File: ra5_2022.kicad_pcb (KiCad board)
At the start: 2 copper layers, 178 parts, among them CN1 KF250-3.5-2P-2, CN2 MX15EDGRHC-3.5-2*02P-BK01-CU-A, CN3 KF250-3.5-2P-2, CN4 KF250-3.5-2P-2, J2 MX15EDGRHC-3.5-2x03P, Q2 BC817, Q3 BC817, Q4 BC817, Q5 BC817, Q6 BC817, U1 TPS54202DDC, U10 DB126V-5.0-2P-BK-P, U11 ISO7741N1-Y, U12 JTD6206-3.3V, U2 B0303S-1WR2, U3 ESP32-C6-MINI-1, U4 AMS1117-3.3, U5 ATM90E32AS-AU-R, U6 K3-2268P, U7 CS817X20LS, U8 ADS1115IDGS, U9 DB126V-5.0-2P-BK-P, Y1 ABM8G-16.384MHZ-18-D2Y-T

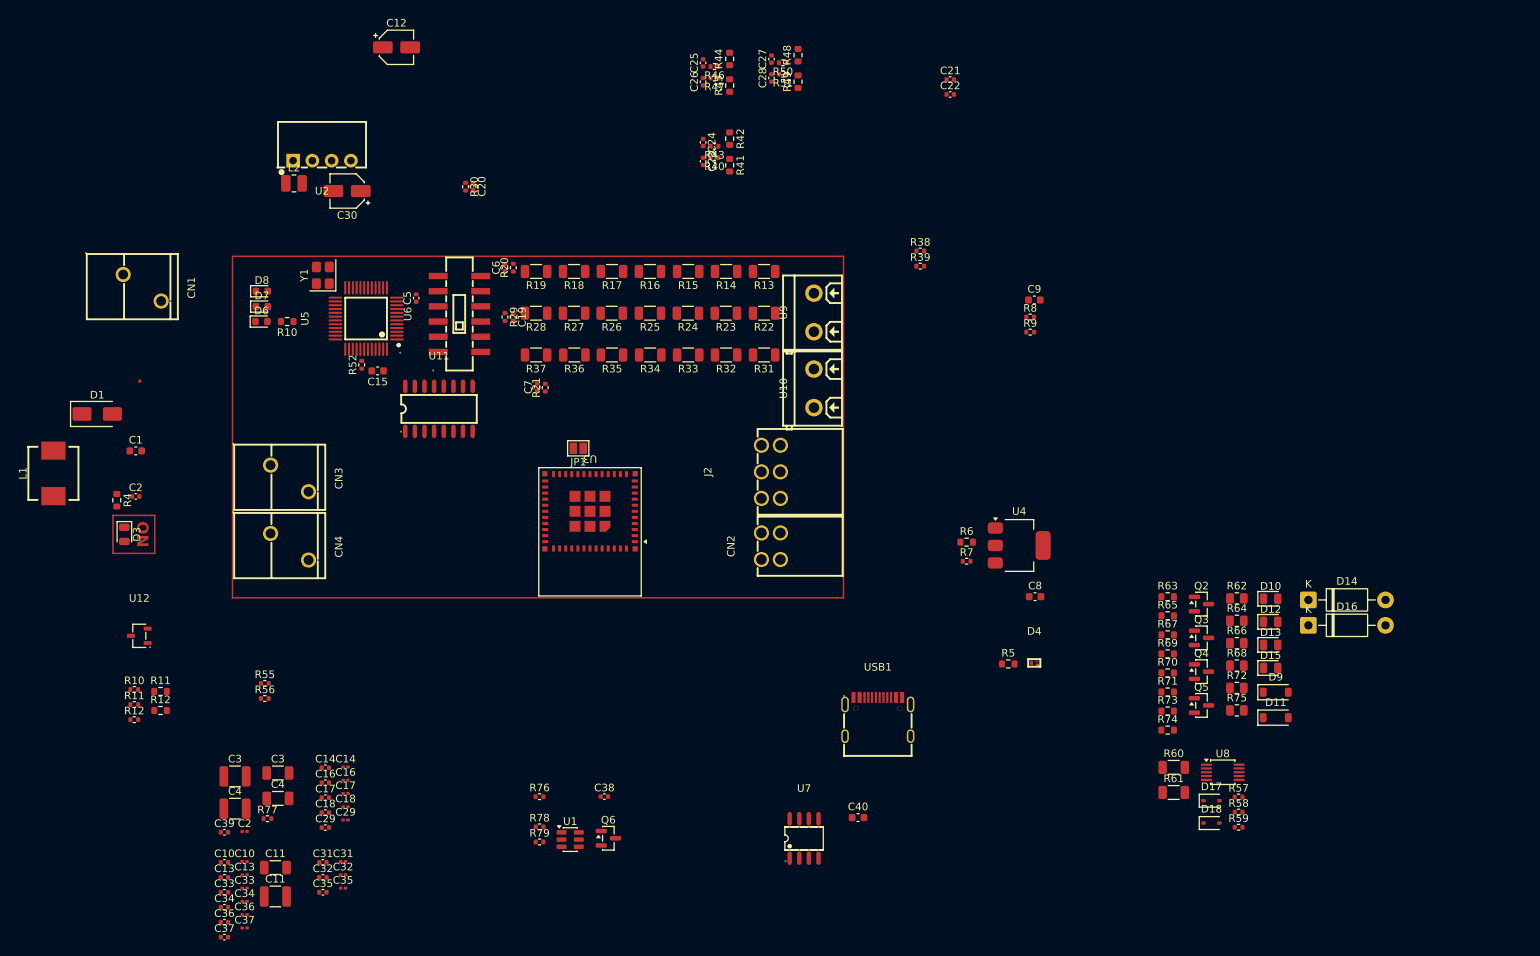
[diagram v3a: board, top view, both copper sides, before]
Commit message: Checkpoint: RA5 base board finished, M.2 shield interconnect defined
Base board (ra5_2022):
- Finalize component placement on ra5_2022.kicad_pcb; next step is routing
- Add STM8S003F3P to bridge the 2 digital inputs / 2 digital outputs onto
  the shared I2C bus (alongside the ADS1115), freeing up M.2 pins
- Wire J1 (M.2 Key-E) to a custom, non-spec-compliant 3.3V pinout: I2C
  (SDA/SCL/ALERT#) on the native pins, M90E32AS SPI reusing the SD/SDIO
  "SPI mode" pin convention (SCLK/MOSI/MISO/CS), PM0/PM1 on VENDOR_DEFINED
  pins, USB-C passthrough, full GND/VDD
- Fix AS0BC21-S40BE-7H footprint: pads 76/77 (shield/ground tabs, not part
  of the 75-pin M.2 spec) remapped onto the GND pin instead of dangling
- Swap the buck inductor (L2) for SLW5040S100MST (C182189): same 10uH,
  lower DCR, 5x5mm footprint to clear a routing constraint
- Remove the unused "Production" KiCad Design Variant and align the
  remaining "Develop" variant's footprints with the defaults -- a
  variant/default footprint mismatch was causing Update PCB from Schematic
  to silently duplicate footprints on every sync
- Clean up 10 further orphaned duplicate footprints left on the PCB from
  earlier design revisions (R11, R12, C14, C16, C17, C18, C29, C31, C32, C35)
- Fix 3D model paths across the shared library to use the RA5_2022_LIB
  environment variable instead of ${KIPRJMOD}, so previews resolve
  correctly from sibling projects too

New sibling project (ra5_shield_modem/):
- MCU + LTE modem card, built to the M.2 Key-E mechanical form factor to
  plug into the base board's J1
- Share the ra5_2022 parts library via sym-lib-table/fp-lib-table
- Add the timonsku/M.2-Card-Footprints submodule as a card-edge template

Co-Authored-By: Claude Sonnet 5 <noreply@anthropic.com>
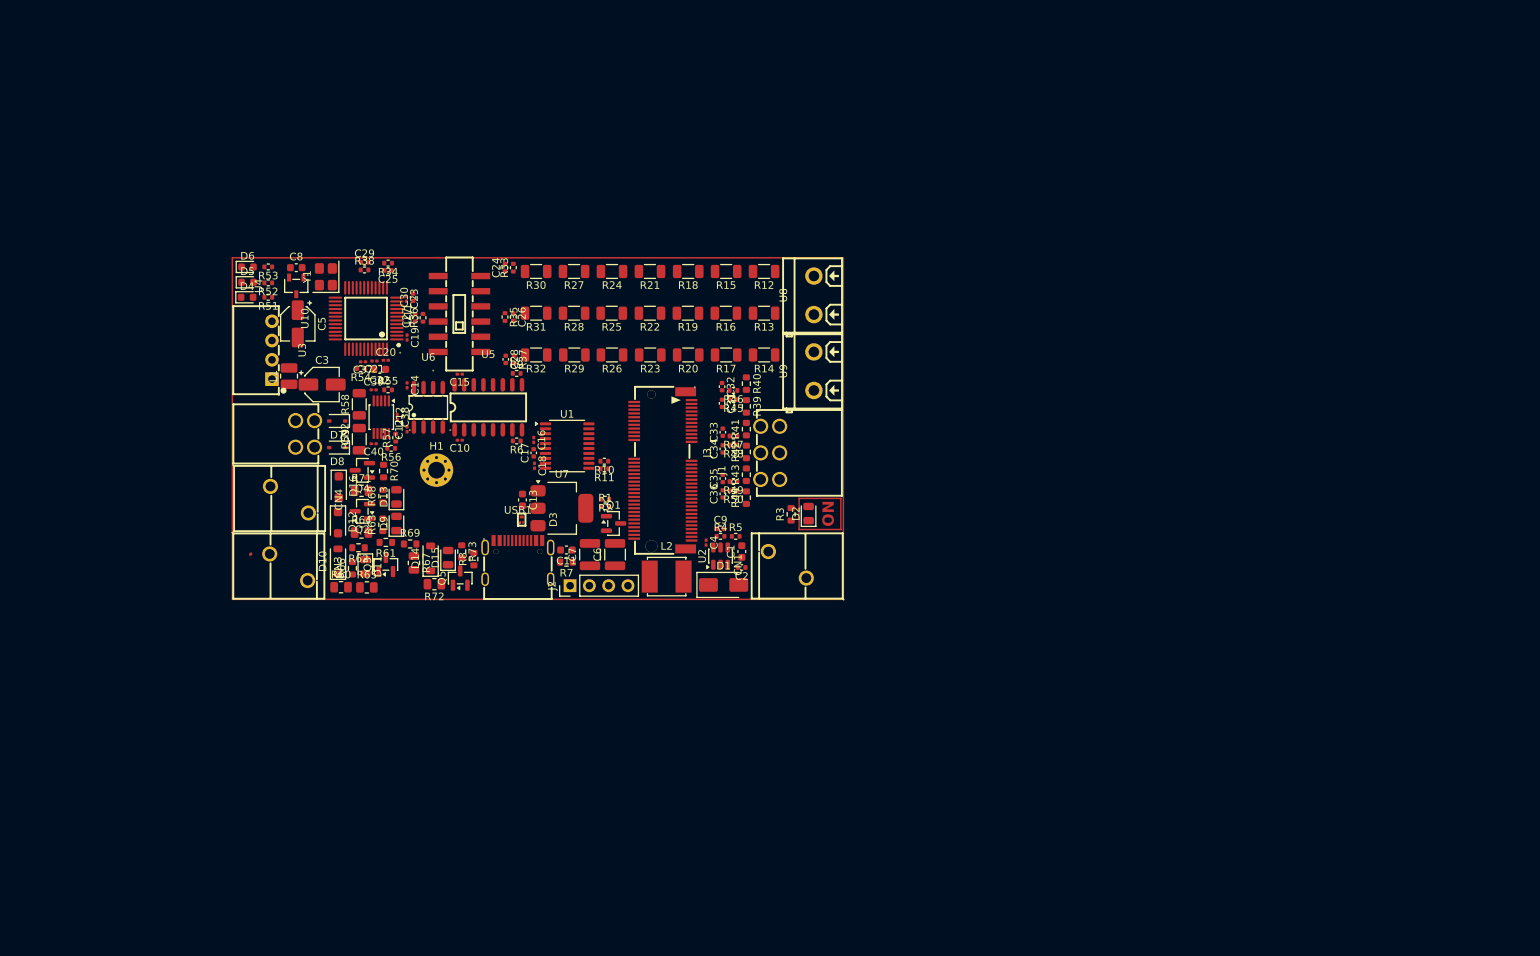
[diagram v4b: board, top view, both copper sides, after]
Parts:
- removed the C10 at (110.1, 153.2)
- removed the C10 at (107.4, 153.4)
- removed the C11 at (114.1, 154.0)
- removed the C11 at (114.1, 157.8)
- removed the C13 at (107.4, 155.3)
- removed the C13 at (110.1, 155.0)
- removed the C2 at (95.8, 105.1)
- removed the C29 at (120.7, 148.8)
- removed the C3 at (108.8, 142.0)
- removed the C3 at (114.5, 141.6)
- removed the C31 at (120.4, 153.4)
- removed the C32 at (120.4, 155.3)
- removed the C33 at (110.1, 156.7)
- removed the C33 at (107.4, 157.3)
- removed the C34 at (107.4, 159.3)
- removed the C34 at (110.1, 158.5)
- removed the C35 at (120.4, 157.3)
- removed the C36 at (107.4, 161.2)
- removed the C36 at (110.1, 160.2)
- removed the C37 at (107.4, 163.2)
- removed the C37 at (110.1, 162.0)
- removed the C4 at (108.8, 146.3)
- removed the C4 at (114.5, 144.9)
- removed the D14 at (250.2, 118.8)
- removed JP1: SolderJumper_2_Open, Jumper:SolderJumper-2_P1.3mm_Open_Pad1.0x1.5mm
- removed the R12 at (99.0, 133.3)
- removed the R7 at (205.2, 113.7)
- removed the R8 at (213.6, 81.5)
- removed the R9 at (213.6, 83.5)
- removed the U3 at (155.6, 107.1)
- added C10: 100nF, Capacitor_SMD:C_0201_0603Metric, F.Cu at (138.4, 97.7)
- added C12: 100nF, Capacitor_SMD:C_0201_0603Metric, F.Cu at (131.5, 96.3)
- added C15: 100nF, Capacitor_SMD:C_0201_0603Metric, F.Cu at (138.4, 89.0)
- added C6: 22uF, Capacitor_SMD:C_1210_3225Metric, F.Cu at (158.9, 112.8)
- added C7: 22uF, Capacitor_SMD:C_1210_3225Metric, F.Cu at (155.6, 112.8)
- added D12: 1N4004W, Diode_SMD:D_SOD-123F, F.Cu at (122.4, 108.6)
- added H1: MountingScrew, MountingHole:MountingHole_2.2mm_M2_Pad_Via, F.Cu at (135.4, 101.7)
- added J1: Bus_M.2_Socket_E, ra5_2022:CONN-SMD_AS0BC21-S48BE-7H, F.Cu at (165.2, 101.7)
- added J2: Conn_01x04_Socket, Connector_PinHeader_2.54mm:PinHeader_1x04_P2.54mm_Vertical, F.Cu at (153.0, 116.9)
- added U1: STM8S003F3P, Package_SO:TSSOP-20_4.4x6.5mm_P0.65mm, F.Cu at (152.6, 98.5)
- C14, C16, C18: footprint Capacitor_SMD:C_0402_1005Metric -> Capacitor_SMD:C_0201_0603Metric
- C17: value 100nF -> 1uF
- D16: footprint Diode_THT:D_DO-41_SOD81_P10.16mm_Horizontal -> Diode_SMD:D_SOD-123F
- L2: renamed from L1; footprint ra5_2022:IND-SMD_L7.0-W6.6 -> ra5_2022:IND-SMD_L5.0-W5.0-1
- R10, R11: value 80R -> 100R; footprint Resistor_SMD:R_0603_1608Metric -> Resistor_SMD:R_0402_1005Metric
- moved D16 129.0 mm to (122.5, 103.9), turned to -90 degrees
- moved D7 125.6 mm to (122.3, 95.2), turned to 180 degrees
- moved D8 125.4 mm to (122.3, 98.7), turned to 180 degrees
- moved D10 124.7 mm to (122.4, 113.7), turned to 90 degrees
- moved R55 124.2 mm to (129.0, 91.1)
- moved R57 122.3 mm to (130.0, 97.4), turned to 90 degrees
- moved R56 121.5 mm to (129.4, 98.8), turned to 180 degrees
- moved U12 120.3 mm to (128.1, 94.7), turned to -90 degrees
- moved D11 119.3 mm to (126.0, 114.4), turned to -90 degrees
- moved R71 118.9 mm to (125.5, 104.4)
- moved R60 118.0 mm to (122.8, 117.1)
- moved R58 117.5 mm to (125.2, 93.0), turned to 90 degrees
- moved D13 117.4 mm to (130.1, 105.2), turned to 90 degrees
- moved R64 117.1 mm to (125.5, 109.9)
- moved R59 117.0 mm to (125.2, 97.6), turned to 90 degrees
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- renumbered C8 to C11, C9 to C13, C14 to C19, C39 to C2, C16 to C20, C17 to C21, C15 to C22, C18 to C23, C6 to C24, C7 to C25, C19 to C26, C20 to C27, C21 to C28, C22 to C29, C12 to C3, C5 to C30, C23 to C31, C24 to C32, C25 to C33, C26 to C34, C27 to C35, C28 to C36, C29 to C37, C31 to C38, C32 to C39, C2 to C4, C35 to C40, C30 to C5, C40 to C8, C38 to C9, D9 to D10, D10 to D11, D15 to D13, D11 to D14, D12 to D15, D3 to D2, D4 to D3, D6 to D4, D7 to D5, D8 to D6, D17 to D7, D18 to D8, D13 to D9, J2 to J3, L2 to L1, Q6 to Q1, Q4 to Q2, Q2 to Q3, Q5 to Q4, Q3 to Q5, R78 to R1, R13 to R12, R22 to R13, R31 to R14, R14 to R15, R23 to R16, R32 to R17, R15 to R18, R24 to R19, R79 to R2, R33 to R20, R16 to R21, R25 to R22, R34 to R23, R17 to R24, R26 to R25, R35 to R26, R18 to R27, R27 to R28, R36 to R29, R4 to R3, R19 to R30, R28 to R31, R37 to R32, R20 to R33, R21 to R34, R29 to R35, R30 to R36, R38 to R37, R39 to R38, R41 to R39, R76 to R4, R42 to R40, R44 to R41, R45 to R42, R48 to R43, R49 to R44, R40 to R45, R43 to R46, R46 to R47, R47 to R48, R50 to R49, R77 to R5, R51 to R50, R10 to R51, R11 to R52, R12 to R53, R52 to R54, R57 to R55, R58 to R56, R59 to R57, R60 to R58, R61 to R59, R55 to R6, R62 to R60, R70 to R61, R63 to R62, R71 to R63, R72 to R64, R64 to R65, R65 to R66, R66 to R67, R73 to R68, R67 to R69, R6 to R7, R74 to R70, R75 to R71, R68 to R72, R69 to R73, R5 to R8, R56 to R9, U5 to U10, U6 to U11, U8 to U12, U1 to U2, U2 to U3, U12 to U4, U11 to U5, U7 to U6, U4 to U7, U9 to U8, U10 to U9
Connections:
- net /MCU/IO15 renamed /MCU/ALERT
- C16 pad 1: GND2 -> /MCU/NRST
- C16 pad 2: VDD2 -> GND
- C17 pad 1: GND2 -> Net-(U1-VCAP)
- C17 pad 2: /MCU/M90E32AS/VDD18 -> GND
- C18 pad 1: GND2 -> VDD
- C18 pad 2: /MCU/M90E32AS/VREF -> GND
- C25 pad 1: /MCU/M90E32AS/V1N -> GND2
- C25 pad 2: GND2 -> /MCU/M90E32AS/V1N
- C27 pad 1: /MCU/M90E32AS/V2N_SW -> GND2
- C27 pad 2: GND2 -> /MCU/M90E32AS/V2N_SW
- C29 pad 1: /MCU/M90E32AS/V3N -> GND2
- C29 pad 2: GND2 -> /MCU/M90E32AS/V3N
- CN3 pad 1: /MCU/Digital IO/DI1 -> /MCU/Digital IO/DI2
- CN3 pad 2: /MCU/Digital IO/DI2 -> /MCU/Digital IO/DI1
- CN4 pad 1: /MCU/Digital IO/DO1 -> /MCU/Digital IO/DO2
- CN4 pad 2: /MCU/Digital IO/DO2 -> /MCU/Digital IO/DO1
- D4 pad 2: Net-(D6-A) (its old number) -> Net-(D4-A)
- D5 pad 2: Net-(D7-A) -> Net-(D5-A)
- R10 pad 1: /MCU/M90E32AS/ZX0 -> /MCU/SCL
- R10 pad 2: Net-(D6-A) (its old number) -> Net-(U1-PB4)
- R11 pad 1: /MCU/M90E32AS/ZX1 -> /MCU/SDA
- R11 pad 2: Net-(D7-A) -> Net-(U1-PB5)
- R34 pad 1: /MCU/M90E32AS/V1N -> GND2
- R34 pad 2: GND2 -> /MCU/M90E32AS/V1N
- R36 pad 1: /MCU/M90E32AS/V2N_SW -> GND2
- R36 pad 2: GND2 -> /MCU/M90E32AS/V2N_SW
- R38 pad 1: /MCU/M90E32AS/V3N -> GND2
- R38 pad 2: GND2 -> /MCU/M90E32AS/V3N
- R51 pad 2: Net-(D6-A) (its old number) -> Net-(D4-A)
- R52 pad 2: Net-(D7-A) -> Net-(D5-A)
- R56 pad 1: /MCU/IO3 -> /MCU/SDA
- R57 pad 1: /MCU/IO2 -> /MCU/SCL
- U10 pad 33: /MCU/PM1 -> /MCU/M90E32AS/PM1
- U10 pad 34: /MCU/PM0 -> /MCU/M90E32AS/PM0
- U12 pad 10: /MCU/IO2 -> /MCU/SCL
- U12 pad 9: /MCU/IO3 -> /MCU/SDA
- U5 pad 3: /MCU/IO21 -> /MCU/CS
- U5 pad 4: /MCU/IO18 -> /MCU/SCLK
- U5 pad 5: /MCU/IO19 -> /MCU/MOSI
- U5 pad 6: /MCU/IO20 -> /MCU/MISO
- U6 pad 2: /MCU/IO0 -> /MCU/PM0
- U6 pad 3: /MCU/IO1 -> /MCU/PM1
- U6 pad 6: /MCU/PM1 -> /MCU/M90E32AS/PM1
- U6 pad 7: /MCU/PM0 -> /MCU/M90E32AS/PM0
